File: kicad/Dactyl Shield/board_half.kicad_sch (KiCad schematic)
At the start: 43 parts, among them J201 JST, J202 Split, J203 Column, J204 Thumb, J205 Foot, J206 Row, J207 Display, J208 Vic, J209 ResA, J212 ResB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

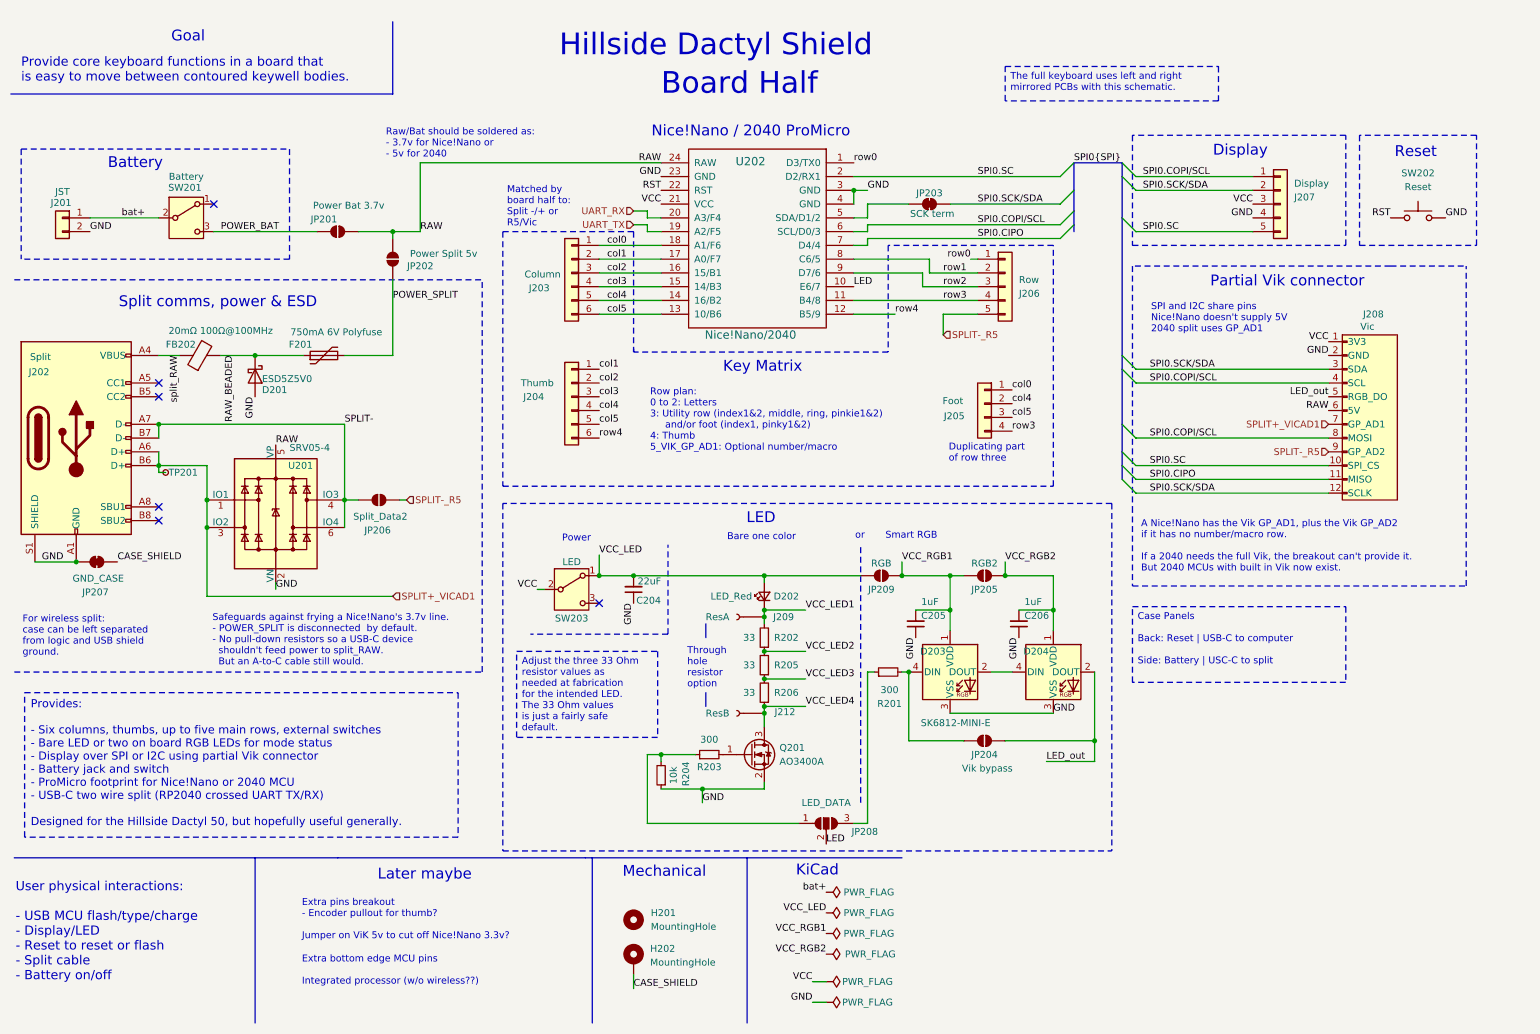
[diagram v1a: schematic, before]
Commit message: feat: key headers match body grid layout (rough)
- Right hand only and just a rought sketch so far
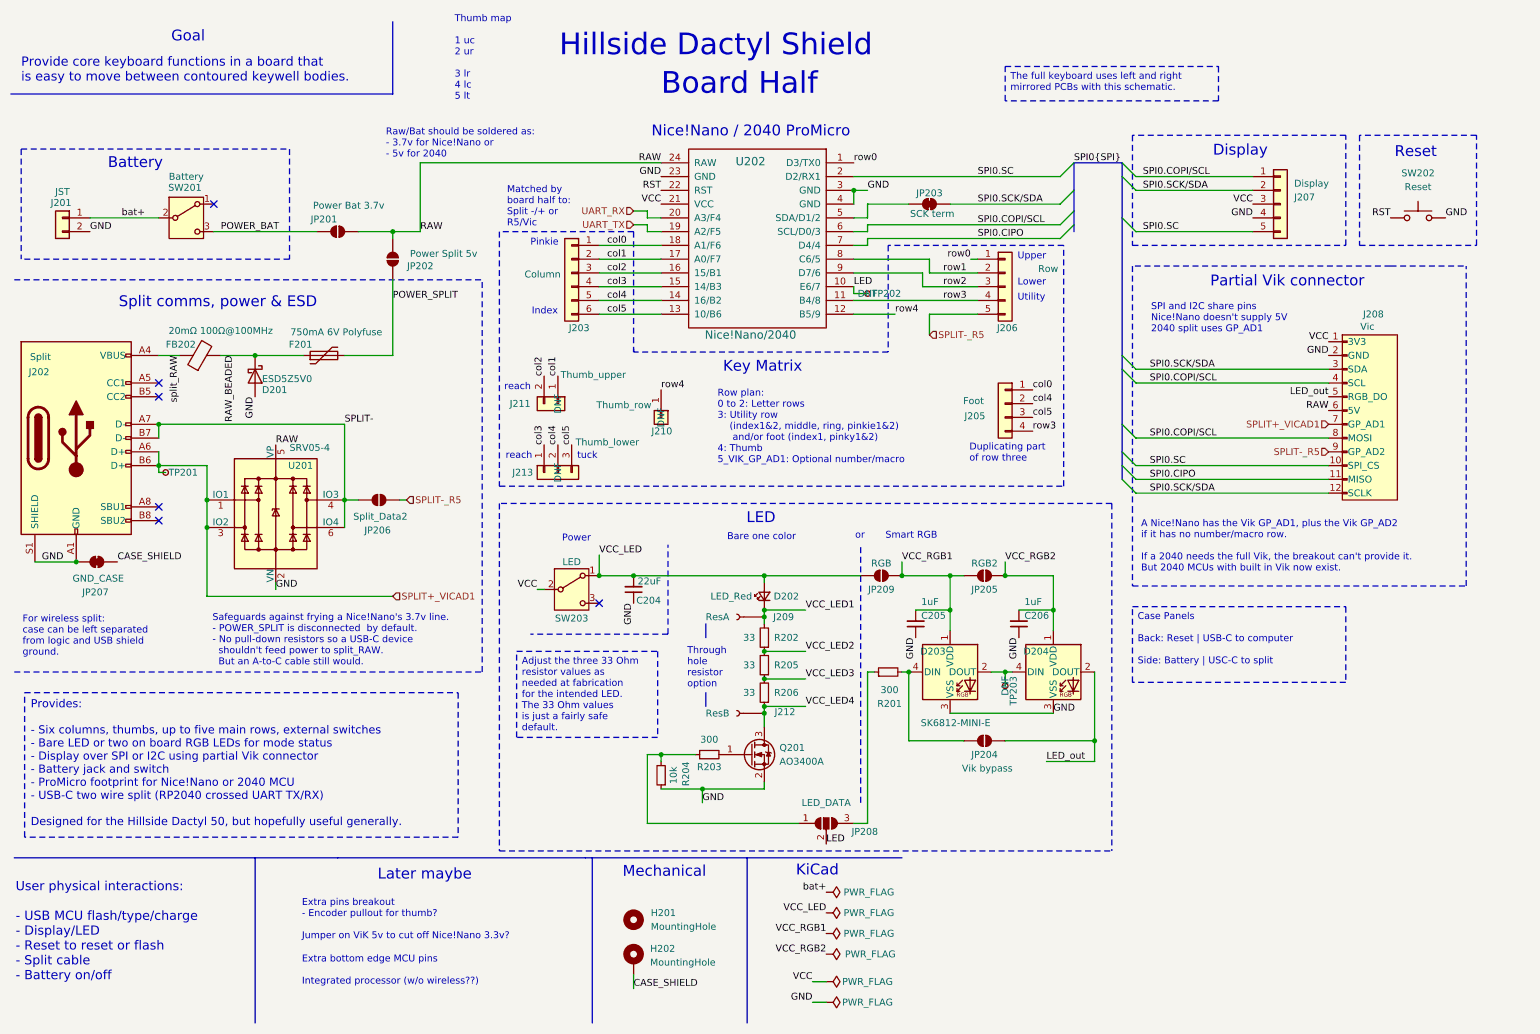
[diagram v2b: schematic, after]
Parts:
- removed J204: Thumb, Dactyl:PinHeader_Thumbs, symbol Connector_Generic:Conn_01x06
- added J210: Thumb_row, Dactyl:PinHeader_Thumb_row, symbol Connector_Generic:Conn_01x01
- added J211: Thumb_upper, Dactyl:PinHeader_Thumb_upper, symbol Connector_Generic:Conn_01x02
- added J213: Thumb_lower, Dactyl:PinHeader_Thumb_lower, symbol Connector_Generic:Conn_01x03
- added TP202, TP203: TestPoint_Small, TestPoint:TestPoint_THTPad_D1.0mm_Drill0.5mm, symbol Connector:TestPoint_Small
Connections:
- net LED: now also TP202.1
- net col1: now also J211.1 (Pin_1)
- net col2: now also J211.2 (Pin_2)
- net col3: now also J213.1 (Pin_1)
- net col4: now also J213.2 (Pin_2)
- net col5: now also J213.3 (Pin_3)
- net row4: now also J210.1 (Pin_1)
- net at D203.2 (DOUT), D204.4 (DIN): now also TP203.1
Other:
- note added: "Index"
- note added: "Lower"
- note added: "Pinkie"
- note added: "Row plan: 0 to 2: Letter rows 3: Utility row (index1&2, middle, ring, pinkie1&2) and/or foot (index1, pinky1&2) 4: Thumb 5_VIK_GP_AD1: Optional number/macro"
- note added: "Thumb map 1 uc 2 ur 3 lr 4 lc 5 lt"
- note added: "Upper"
- note added: "Utility"
- note added: "reach"
- note added: "tuck"
- note removed: "Row plan: 0 to 2: Letters 3: Utility row (index1&2, middle, ring, pinkie1&2) and/or foot (index1, pinky1&2) 4: Thumb 5_VIK_GP_AD1: Optional number/macro"
- moved on the sheet: J205

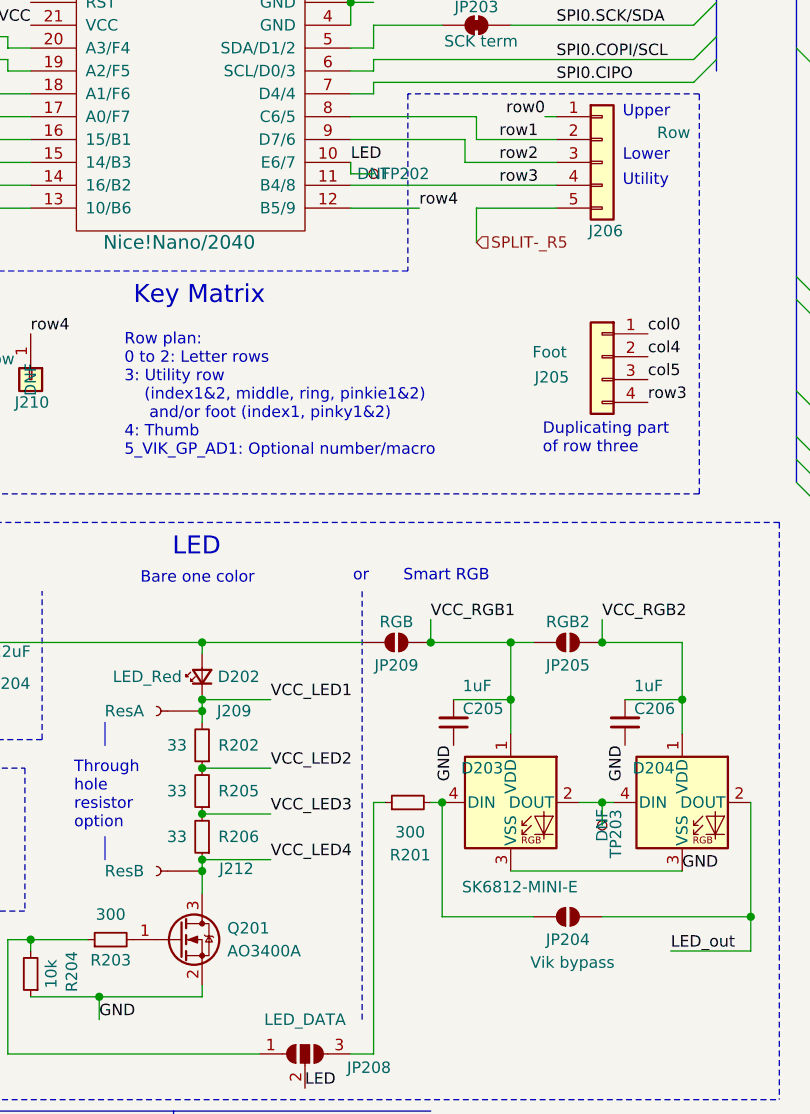
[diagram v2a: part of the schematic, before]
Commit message: feat: move LED test point
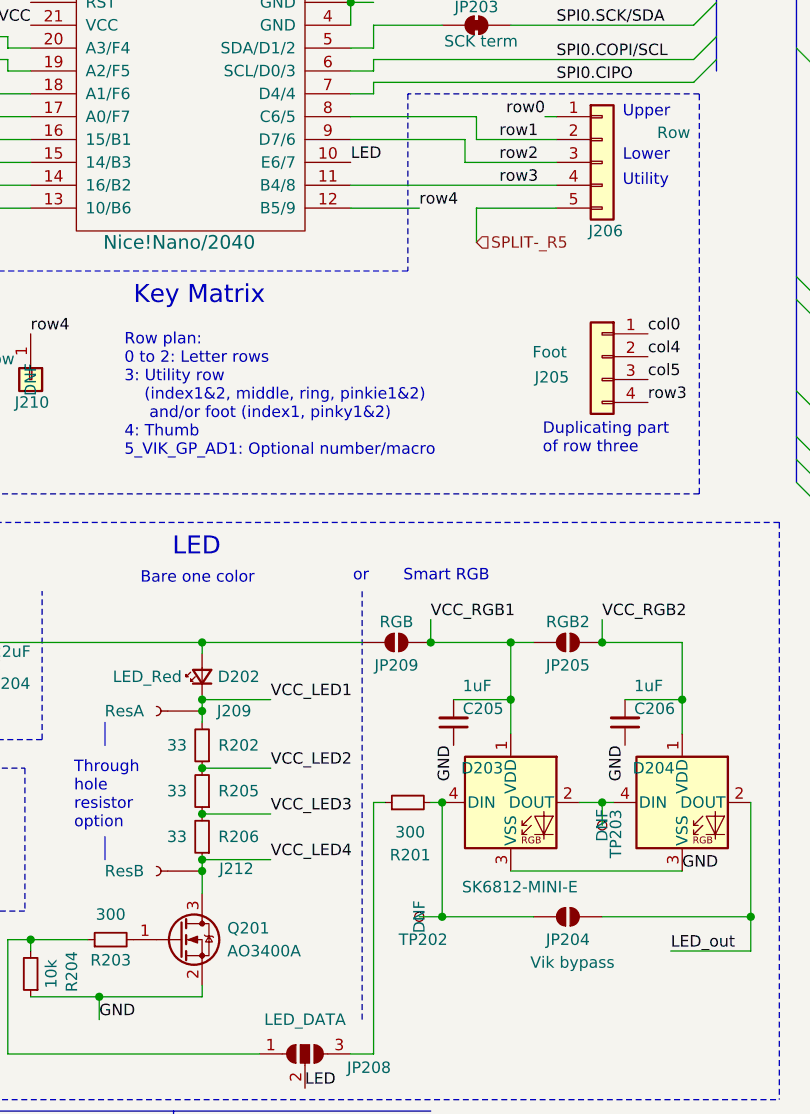
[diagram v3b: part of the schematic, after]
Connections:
- net LED: no longer TP202.1
- net at D203.4 (DIN), JP204.1 (A), R201.2: now also TP202.1
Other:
- moved on the sheet: TP202
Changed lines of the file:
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@@
 	)
 	(junction
+		(at 177.8 144.78)
+		(diameter 0)
+		(color 0 0 0 0)
+	)
+	(junction
 		(at 39.37 93.98)
 		(diameter 0)
@@
 		)
 	)
+	(wire
+		(pts
+			(xy 175.26 144.78) (xy 177.8 144.78)
+		)
+		(stroke
+			(width 0)
+			(type default)
+		)
+	)
 	(polyline
 		(pts
@@
 		)
 	)
-	(wire
-		(pts
-			(xy 167.64 62.23) (xy 167.64 60.96)
-		)
-		(stroke
-			(width 0)
-			(type default)
-		)
-	)
 	(polyline
 		(pts
@@
 	(wire
 		(pts
-			(xy 167.64 62.23) (xy 170.18 62.23)
-		)
-		(stroke
-			(width 0)
-			(type default)
-		)
-	)
-	(wire
-		(pts
 			(xy 127 46.99) (xy 129.54 46.99)
 		)
@@
 	(symbol
 		(lib_id "Connector:TestPoint_Small")
-		(at 170.18 62.23 0)
+		(at 175.26 144.78 270)
 		(unit 1)
 		(exclude_from_sim no)
@@
 		(dnp no)
 		(property "Reference" "TP202"
-			(at 170.942 62.23 0)
+			(at 172.974 147.32 90)
 			(effects
 				(font
@@
 		)
 		(property "Value" "TestPoint_Small"
-			(at 171.45 63.4999 0)
+			(at 173.9901 146.05 0)
 			(effects
 				(font
@@
 		)
 		(property "Footprint" "TestPoint:TestPoint_THTPad_D1.0mm_Drill0.5mm"
-			(at 175.26 62.23 0)
+			(at 175.26 149.86 0)
 			(effects
 				(font
@@
 		)
 		(property "Datasheet" "~"
-			(at 175.26 62.23 0)
+			(at 175.26 149.86 0)
 			(effects
 				(font
@@
 		)
 		(property "Description" "test point"
-			(at 170.18 62.23 0)
+			(at 175.26 144.78 0)
 			(effects
 				(font
@@
 		)
 		(property "Config" "DNF"
-			(at 170.18 62.23 0)
+			(at 175.26 144.78 0)
 			(effects
 				(font

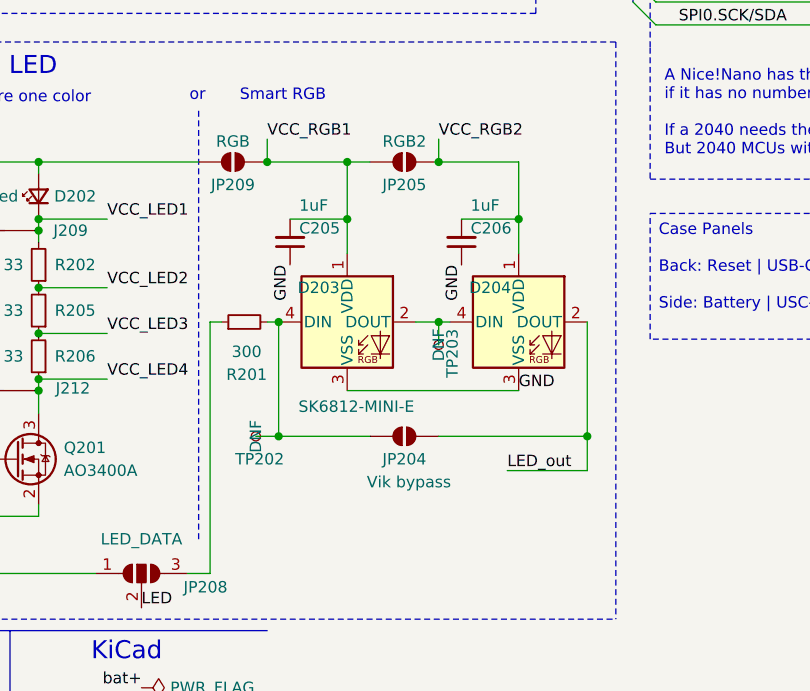
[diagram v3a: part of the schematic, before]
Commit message: feat: left side wired and passes
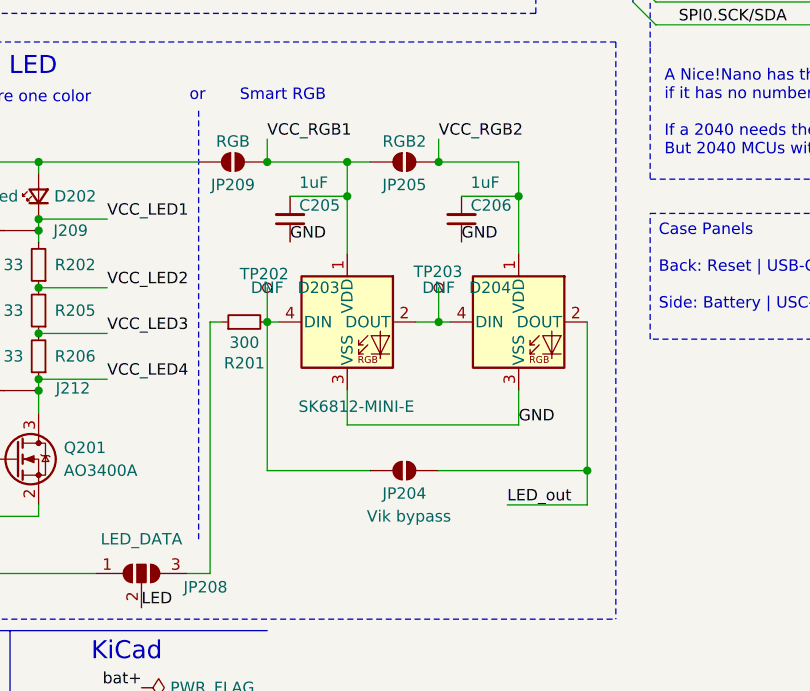
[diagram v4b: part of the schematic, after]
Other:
- moved on the sheet: C205, C206, JP204, TP202, TP203

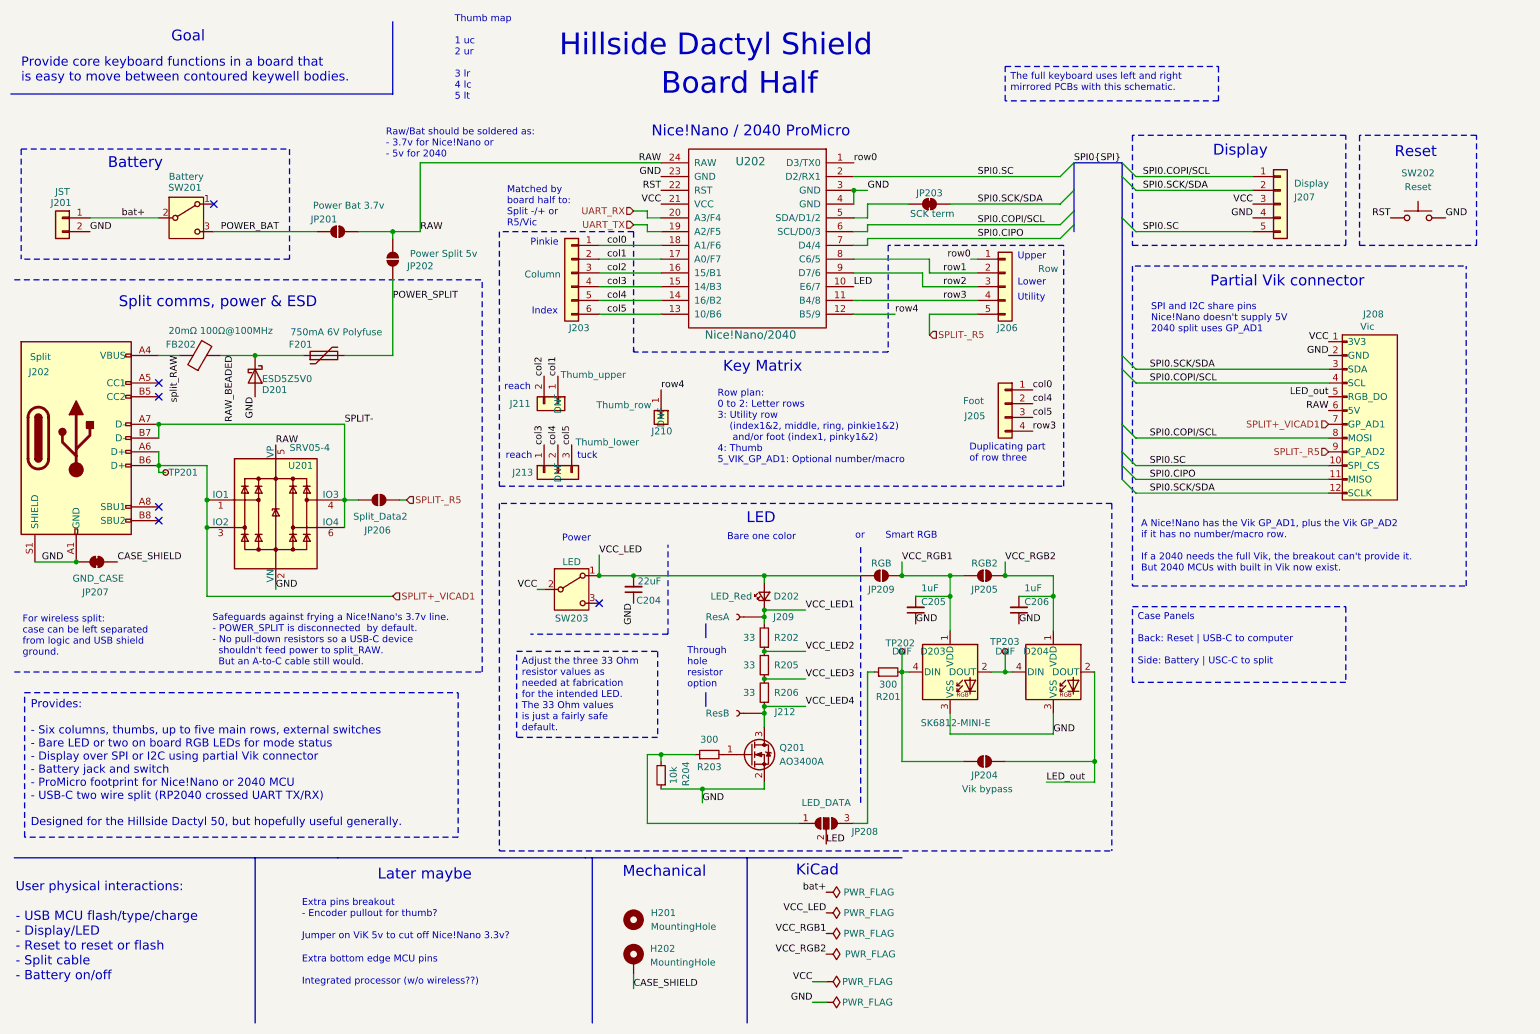
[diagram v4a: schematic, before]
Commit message: feat(schematic): clean up warnings
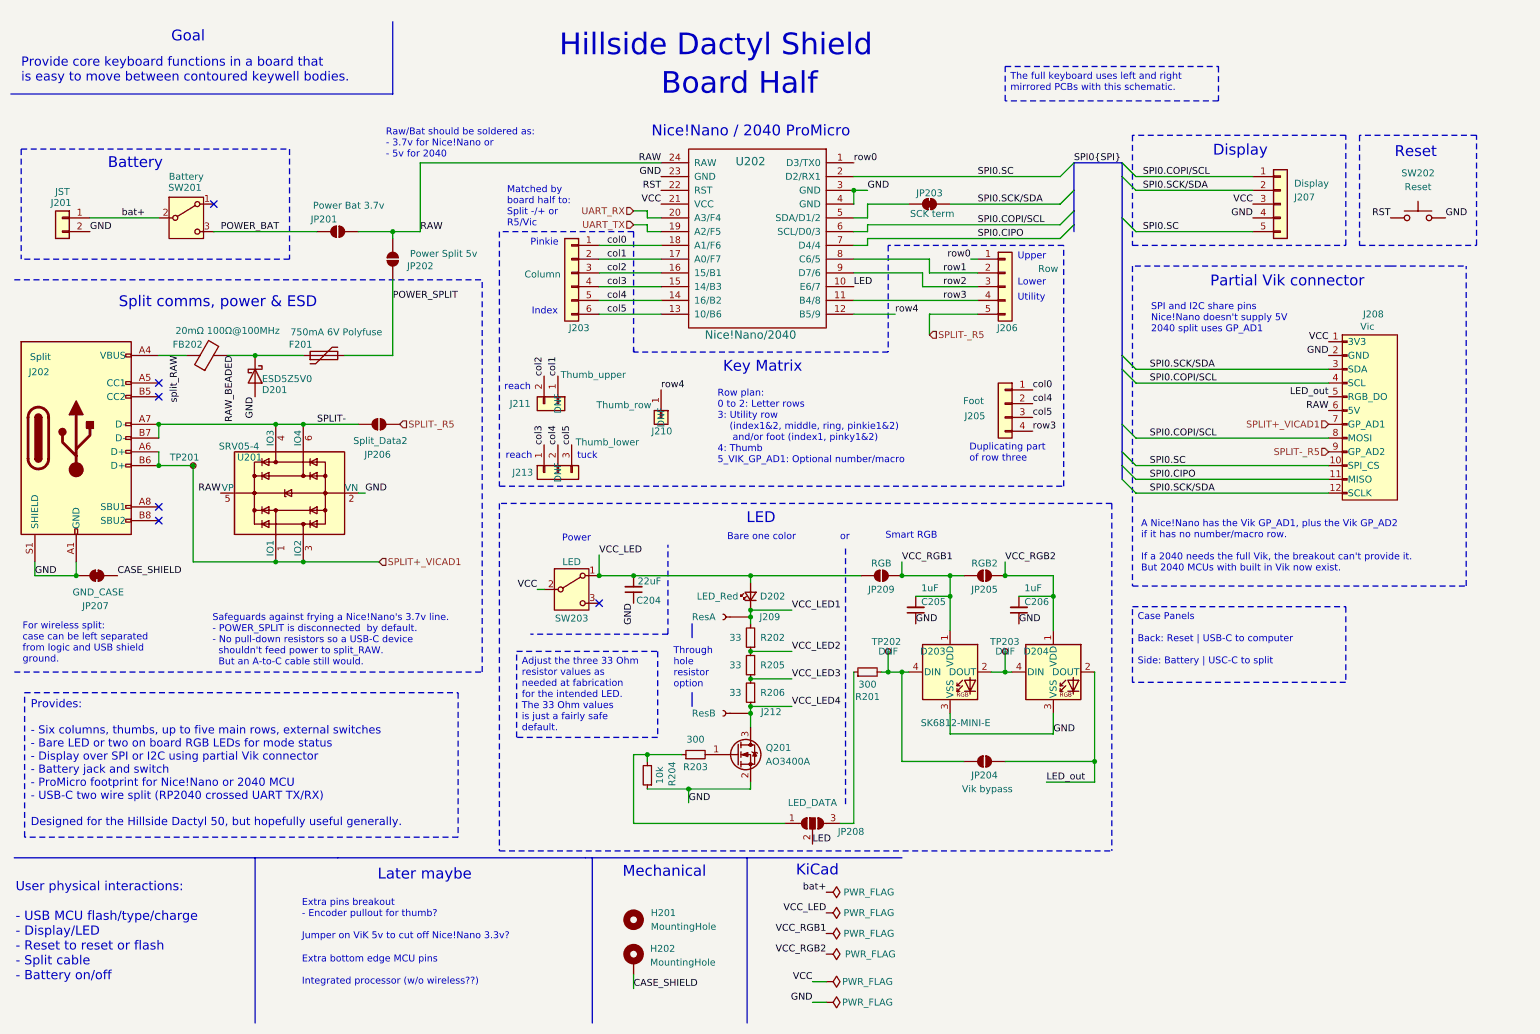
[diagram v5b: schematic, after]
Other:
- note removed: "Thumb map 1 uc 2 ur 3 lr 4 lc 5 lt"
- moved on the sheet: D202, FB202, J209, J212, JP206, JP207, JP208, Q201, R201, R202, R203, R204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
